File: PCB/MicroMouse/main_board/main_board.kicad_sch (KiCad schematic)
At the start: 1 part, among them U1 ESP32-WROOM-32

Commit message: PCB prototype
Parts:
- removed U1: ESP32-WROOM-32, RF_Module:ESP32-WROOM-32, symbol RF_Module:ESP32-WROOM-32
- added C1: 1u, Capacitor_SMD:C_0603_1608Metric, symbol RC_station1_3-eagle-import:C-EUC0603K
- added C2: 100n, Capacitor_SMD:C_0603_1608Metric, symbol RC_station1_3-eagle-import:C-EUC0603K
- added C3: 10n, Capacitor_SMD:C_0603_1608Metric, symbol RC_station1_3-eagle-import:C-EUC0603K
- added C4: 10p, Capacitor_SMD:C_0603_1608Metric, symbol RC_station1_3-eagle-import:C-EUC0603K
- added C5: 22u, Capacitor_SMD:C_1206_3216Metric, symbol RC_station1_3-eagle-import:C-EUC1206K
- added C6: 4.7u, Capacitor_Tantalum_SMD:CP_EIA-7343-15_Kemet-W, symbol Device:C_Polarized
- added C7: 100u, Capacitor_SMD:CP_Elec_6.3x7.7, symbol Device:C_Polarized
- added C8, C9: C, Capacitor_SMD:C_0603_1608Metric, symbol Device:C
- added J1: Conn_01x06, Connector_Molex:Molex_SPOX_5267-06A_1x06_P2.50mm_Vertical, symbol Connector_Generic:Conn_01x06
- added J2, J3: Conn_01x06, Connector_Molex:Molex_KK-254_AE-6410-06A_1x06_P2.54mm_Vertical, symbol Connector_Generic:Conn_01x06
- added L1: 2.2uH, Inductor_SMD:L_1210_3225Metric, symbol RC_station1_3-eagle-import:L-EUL3225M
- added R1: 18.2k, Resistor_SMD:R_0603_1608Metric, symbol RC_station1_3-eagle-import:R-EU_R0603
- added R2: 100k, Resistor_SMD:R_0603_1608Metric, symbol RC_station1_3-eagle-import:R-EU_R0603
- added R3: 309K, Resistor_SMD:R_0603_1608Metric, symbol RC_station1_3-eagle-import:R-EU_R0603
- added R4: 1M, Resistor_SMD:R_0603_1608Metric, symbol RC_station1_3-eagle-import:R-EU_R0603
- added R6: R, Resistor_SMD:R_0603_1608Metric, symbol Device:R
- added U2: LT8608, Package_SO:MSOP-10-1EP_3x3mm_P0.5mm_EP1.68x1.88mm, symbol RC_station1_3-eagle-import:LT8608
- added U3: TB6612FNG, Package_SO:SSOP-24_5.3x8.2mm_P0.65mm, symbol Driver_Motor:TB6612FNG
- added U4: ESP32-WROOM-32U, RF_Module:ESP32-WROOM-32U, symbol RF_Module:ESP32-WROOM-32U
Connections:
- new net: C4.1, R3.2, R4.2, U2.6 (FB)
- new net: C2.2, L1.2, U2.2 (SW)
- new net: C1.1, U2.3 (INTVCC)
- new net: C2.1, U2.1 (BST)
- new net: R1.2, U2.4 (RT)
- new net: C3.1, U2.7 (TR/SS)
- new net: R2.2, U2.8 (PG)
- new net +3V3: C8.1, C9.1, J1.6 (Pin_6), U4.2 (VDD)
- new net +6V: C4.2, C5.1, L1.1, R2.1, R4.1, U3.13 (VM2), U3.14 (VM3), U3.20 (VCC), U3.24 (VM1)
- new net CTS: J1.1 (Pin_1), U4.25 (IO0)
- new net GND: C1.2, C3.2, C5.2, C6.2, C7.2, C9.2, J1.5 (Pin_5), R1.1, R3.1, R6.2, U2.11 (GND), U2.5 (SYNC), U3.10 (PGND2), U3.18 (GND), U3.3 (PGND1), U3.4 (PGND1), U3.9 (PGND2), U4.1 (GND), U4.15 (GND), U4.38 (GND), U4.39 (GND)
- new net HALL+: J2.5 (Pin_5), J3.5 (Pin_5)
- new net HALL-: J2.6 (Pin_6), J3.6 (Pin_6)
- new net HALL_MOTORA_A: J2.3 (Pin_3)
- new net HALL_MOTORA_B: J2.4 (Pin_4)
- new net HALL_MOTORB_A: J3.3 (Pin_3)
- new net HALL_MOTORB_B: J3.4 (Pin_4)
- new net IN1A: U3.21 (AIN1), U4.12 (IO27)
- new net IN1B: U3.22 (AIN2), U4.11 (IO26)
- new net IN2A: U3.17 (BIN1), U4.14 (IO12)
- new net IN2B: U3.16 (BIN2), U4.29 (IO5)
- new net MOTORA+: J2.1 (Pin_1), U3.1 (AO1), U3.2 (AO1)
- new net MOTORA-: J2.2 (Pin_2), U3.5 (AO2), U3.6 (AO2)
- new net MOTORB+: J3.1 (Pin_1), U3.11 (BO1), U3.12 (BO1)
- new net MOTORB-: J3.2 (Pin_2), U3.7 (BO2), U3.8 (BO2)
- new net PWMA: U3.23 (PWMA), U4.10 (IO25)
- new net PWMB: U3.15 (PWMB), U4.16 (IO13)
- new net RTS: C8.2, J1.2 (Pin_2), R6.1, U4.3 (EN)
- new net RXD: J1.4 (Pin_4), U4.34 (RXD0/IO3)
- new net TXD: J1.3 (Pin_3), U4.35 (TXD0/IO1)
- new net VCC: C6.1, C7.1, U2.10 (EN/UV), U2.9 (VIN)
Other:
- note added: "Napajacia cast"
- note added: "Prepocitat na 6V"

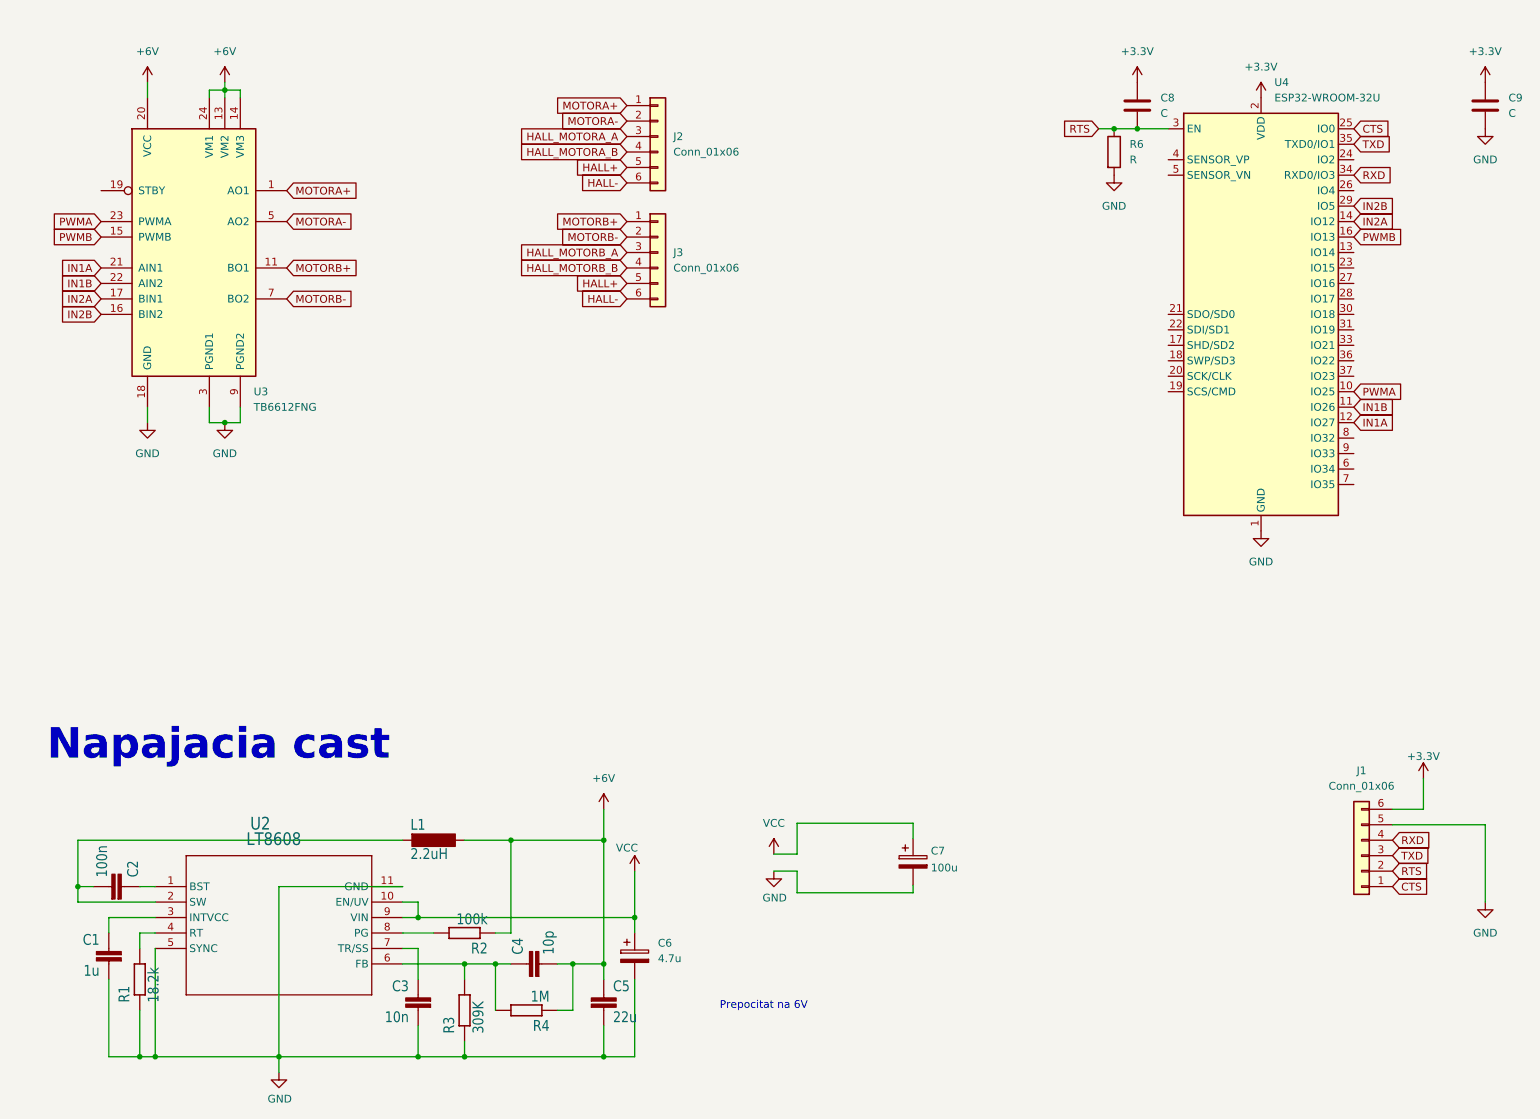
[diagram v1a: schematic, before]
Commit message: atmel328p for reading ToF sensors
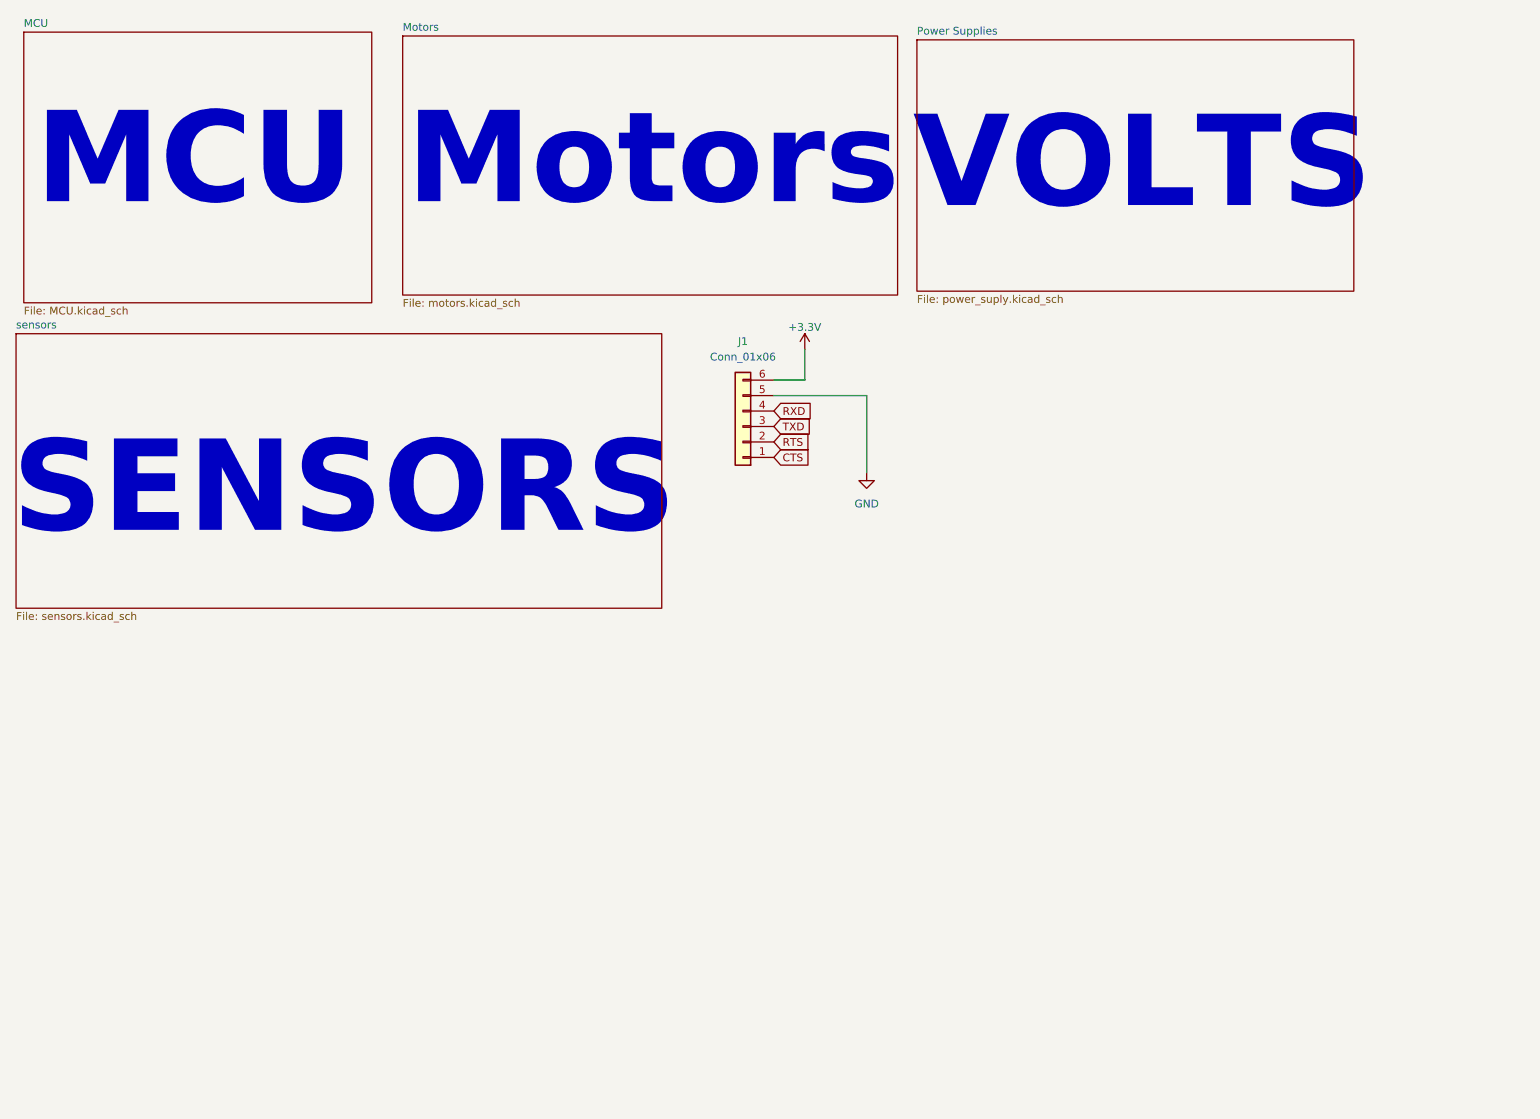
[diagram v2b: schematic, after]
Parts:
- removed C1: 1u, Capacitor_SMD:C_0603_1608Metric, symbol RC_station1_3-eagle-import:C-EUC0603K
- removed C2: 100n, Capacitor_SMD:C_0603_1608Metric, symbol RC_station1_3-eagle-import:C-EUC0603K
- removed C3: 10n, Capacitor_SMD:C_0603_1608Metric, symbol RC_station1_3-eagle-import:C-EUC0603K
- removed C4: 10p, Capacitor_SMD:C_0603_1608Metric, symbol RC_station1_3-eagle-import:C-EUC0603K
- removed C5: 22u, Capacitor_SMD:C_1206_3216Metric, symbol RC_station1_3-eagle-import:C-EUC1206K
- removed C6: 4.7u, Capacitor_Tantalum_SMD:CP_EIA-7343-15_Kemet-W, symbol Device:C_Polarized
- removed C7: 100u, Capacitor_SMD:CP_Elec_6.3x7.7, symbol Device:C_Polarized
- removed C8, C9: C, Capacitor_SMD:C_0603_1608Metric, symbol Device:C
- removed J2, J3: Conn_01x06, Connector_Molex:Molex_KK-254_AE-6410-06A_1x06_P2.54mm_Vertical, symbol Connector_Generic:Conn_01x06
- removed L1: 2.2uH, Inductor_SMD:L_1210_3225Metric, symbol RC_station1_3-eagle-import:L-EUL3225M
- removed R1: 18.2k, Resistor_SMD:R_0603_1608Metric, symbol RC_station1_3-eagle-import:R-EU_R0603
- removed R2: 100k, Resistor_SMD:R_0603_1608Metric, symbol RC_station1_3-eagle-import:R-EU_R0603
- removed R3: 309K, Resistor_SMD:R_0603_1608Metric, symbol RC_station1_3-eagle-import:R-EU_R0603
- removed R4: 1M, Resistor_SMD:R_0603_1608Metric, symbol RC_station1_3-eagle-import:R-EU_R0603
- removed R6: R, Resistor_SMD:R_0603_1608Metric, symbol Device:R
- removed U2: LT8608, Package_SO:MSOP-10-1EP_3x3mm_P0.5mm_EP1.68x1.88mm, symbol RC_station1_3-eagle-import:LT8608
- removed U3: TB6612FNG, Package_SO:SSOP-24_5.3x8.2mm_P0.65mm, symbol Driver_Motor:TB6612FNG
- removed U4: ESP32-WROOM-32U, RF_Module:ESP32-WROOM-32U, symbol RF_Module:ESP32-WROOM-32U
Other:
- added sheet MCU (MCU.kicad_sch)
- added sheet Motors (motors.kicad_sch)
- added sheet Power Supplies (power_suply.kicad_sch)
- added sheet sensors (sensors.kicad_sch)
- note added: "MCU"
- note added: "Motors"
- note added: "SENSORS"
- note added: "VOLTS"
- note removed: "Napajacia cast"
- note removed: "Prepocitat na 6V"
- moved on the sheet: J1

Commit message: second PCB
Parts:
- added H1, H2, H3, H4: MountingHole, MountingHole:MountingHole_2.7mm_M2.5_DIN965_Pad, symbol Mechanical:MountingHole
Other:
- removed sheet Motors
- note removed: "Motors"
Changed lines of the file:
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@@
     (stroke (width 0) (type default))
   )
-  (text "Motors" (at 80.645 46.99 0)
-    (effects (font (size 15 15) (thickness 3) bold) (justify left bottom))
-  )
-  (text "VOLTS\n" (at 163.83 47.625 0)
+  (text "VOLTS\n" (at 76.835 47.498 0)
     (effects (font (size 15 15) (thickness 3) bold) (justify left bottom))
   )
@@
     (property "Intersheetrefs" "${INTERSHEET_REFS}" (at 147.4023 84.455 0)
       (effects (font (size 1.27 1.27)) (justify left) hide)
+    )
+  )
+  (symbol (lib_id "Mechanical:MountingHole") (at 129.667 119.761 0) (unit 1)
+    (in_bom yes) (on_board yes) (dnp no) (fields_autoplaced)
+    (property "Reference" "H3" (at 133.223 118.491 0)
+      (effects (font (size 1.27 1.27)) (justify left))
+    )
+    (property "Value" "MountingHole" (at 133.223 121.031 0)
+      (effects (font (size 1.27 1.27)) (justify left))
+    )
+    (property "Footprint" "MountingHole:MountingHole_2.7mm_M2.5_DIN965_Pad" (at 129.667 119.761 0)
+      (effects (font (size 1.27 1.27)) hide)
+    )
+    (property "Datasheet" "~" (at 129.667 119.761 0)
+      (effects (font (size 1.27 1.27)) hide)
+    )
+    (instances
+      (project "main_board"
+        (path "/3863100a-f026-49db-8424-2d27c05016cc"
+          (reference "H3") (unit 1)
+        )
+      )
+    )
+  )
+  (symbol (lib_id "Mechanical:MountingHole") (at 129.667 125.476 0) (unit 1)
+    (in_bom yes) (on_board yes) (dnp no) (fields_autoplaced)
+    (property "Reference" "H4" (at 133.223 124.206 0)
+      (effects (font (size 1.27 1.27)) (justify left))
+    )
+    (property "Value" "MountingHole" (at 133.223 126.746 0)
+      (effects (font (size 1.27 1.27)) (justify left))
+    )
+    (property "Footprint" "MountingHole:MountingHole_2.7mm_M2.5_DIN965_Pad" (at 129.667 125.476 0)
+      (effects (font (size 1.27 1.27)) hide)
+    )
+    (property "Datasheet" "~" (at 129.667 125.476 0)
+      (effects (font (size 1.27 1.27)) hide)
+    )
+    (instances
+      (project "main_board"
+        (path "/3863100a-f026-49db-8424-2d27c05016cc"
+          (reference "H4") (unit 1)
+        )
+      )
     )
   )
@@
     )
   )
-  (sheet (at 164.465 18.415) (size 71.755 41.275) (fields_autoplaced)
+  (symbol (lib_id "Mechanical:MountingHole") (at 129.794 109.474 0) (unit 1)
+    (in_bom yes) (on_board yes) (dnp no) (fields_autoplaced)
+    (property "Reference" "H1" (at 133.35 108.204 0)
+      (effects (font (size 1.27 1.27)) (justify left))
+    )
+    (property "Value" "MountingHole" (at 133.35 110.744 0)
+      (effects (font (size 1.27 1.27)) (justify left))
+    )
+    (property "Footprint" "MountingHole:MountingHole_2.7mm_M2.5_DIN965_Pad" (at 129.794 109.474 0)
+      (effects (font (size 1.27 1.27)) hide)
+    )
+    (property "Datasheet" "~" (at 129.794 109.474 0)
+      (effects (font (size 1.27 1.27)) hide)
+    )
+    (instances
+      (project "main_board"
+        (path "/3863100a-f026-49db-8424-2d27c05016cc"
+          (reference "H1") (unit 1)
+        )
+      )
+    )
+  )
+  (symbol (lib_id "Mechanical:MountingHole") (at 129.667 114.808 0) (unit 1)
+    (in_bom yes) (on_board yes) (dnp no) (fields_autoplaced)
+    (property "Reference" "H2" (at 133.223 113.538 0)
+      (effects (font (size 1.27 1.27)) (justify left))
+    )
+    (property "Value" "MountingHole" (at 133.223 116.078 0)
+      (effects (font (size 1.27 1.27)) (justify left))
+    )
+    (property "Footprint" "MountingHole:MountingHole_2.7mm_M2.5_DIN965_Pad" (at 129.667 114.808 0)
+      (effects (font (size 1.27 1.27)) hide)
+    )
+    (property "Datasheet" "~" (at 129.667 114.808 0)
+      (effects (font (size 1.27 1.27)) hide)
+    )
+    (instances
+      (project "main_board"
+        (path "/3863100a-f026-49db-8424-2d27c05016cc"
+          (reference "H2") (unit 1)
+        )
+      )
+    )
+  )
+  (sheet (at 77.47 18.288) (size 71.755 41.275) (fields_autoplaced)
     (stroke (width 0.1524) (type solid))
     (fill (color 0 0 0 0.0000))
-    (property "Sheetname" "Power Supplies" (at 164.465 17.7034 0)
+    (property "Sheetname" "Power Supplies" (at 77.47 17.5764 0)
       (effects (font (size 1.27 1.27)) (justify left bottom))
     )
-    (property "Sheetfile" "power_suply.kicad_sch" (at 164.465 60.2746 0)
+    (property "Sheetfile" "power_suply.kicad_sch" (at 77.47 60.1476 0)
       (effects (font (size 1.27 1.27)) (justify left top))
     )
@@
       )
     )
-  )
-  (sheet (at 80.01 17.78) (size 81.28 42.545) (fields_autoplaced)
-    (stroke (width 0.1524) (type solid))
-    (fill (color 0 0 0 0.0000))
-    (property "Sheetname" "Motors" (at 80.01 17.0684 0)
-      (effects (font (size 1.27 1.27)) (justify left bottom))
-    )
-    (property "Sheetfile" "motors.kicad_sch" (at 80.01 60.9096 0)
-      (effects (font (size 1.27 1.27)) (justify left top))
-    )
-    (instances
-      (project "main_board"
-        (path "/3863100a-f026-49db-8424-2d27c05016cc" (page "3"))
-      )
-    )

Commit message: PCB prototype
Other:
- added sheet Motors (motors.kicad_sch)
- note added: "Motors"
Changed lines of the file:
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@@
     (stroke (width 0) (type default))
+  )
+  (text "Motors" (at 155.575 45.847 0)
+    (effects (font (size 15 15) (thickness 3) bold) (justify left bottom))
   )
   (text "VOLTS\n" (at 76.835 47.498 0)
@@
     )
   )
+  (sheet (at 154.94 16.637) (size 81.28 42.545) (fields_autoplaced)
+    (stroke (width 0.1524) (type solid))
+    (fill (color 0 0 0 0.0000))
+    (property "Sheetname" "Motors" (at 154.94 15.9254 0)
+      (effects (font (size 1.27 1.27)) (justify left bottom))
+    )
+    (property "Sheetfile" "motors.kicad_sch" (at 154.94 59.7666 0)
+      (effects (font (size 1.27 1.27)) (justify left top))
+    )
+  )

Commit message: ready for manufacture
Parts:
- added H10, H11, H12, H13, H14, H15, H16, H17, H18, H19, H20, H5, H6, H7, H8, H9: MountingHole, MountingHole:MountingHole_2.7mm_M2.5_DIN965_Pad, symbol Mechanical:MountingHole
